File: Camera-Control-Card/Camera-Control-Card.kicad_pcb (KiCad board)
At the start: 4 copper layers, 65 x 41.6 mm, 129 parts, among them J1 SFV24R-1STE1HLF, J2 Conn_02x05_Counter_Clockwise, J3 Conn_Coaxial, J4 Conn_Coaxial, J5 Conn_Coaxial, J6 Conn_Coaxial, J7 Conn_Coaxial, J8 10018784-10201TLF, J9 USB_C_Receptacle_USB2.0_16P, U1 LCMXO2-7000HC-6TG144I, U2 T602-025.0M, U3 SN74LVC1G125DRL, U4 74AHC125, U5 74AHC125, U6 TPD2EUSB30, U7 CP2102N-Axx-xQFN20, U8 SN74LVC1G125DRL

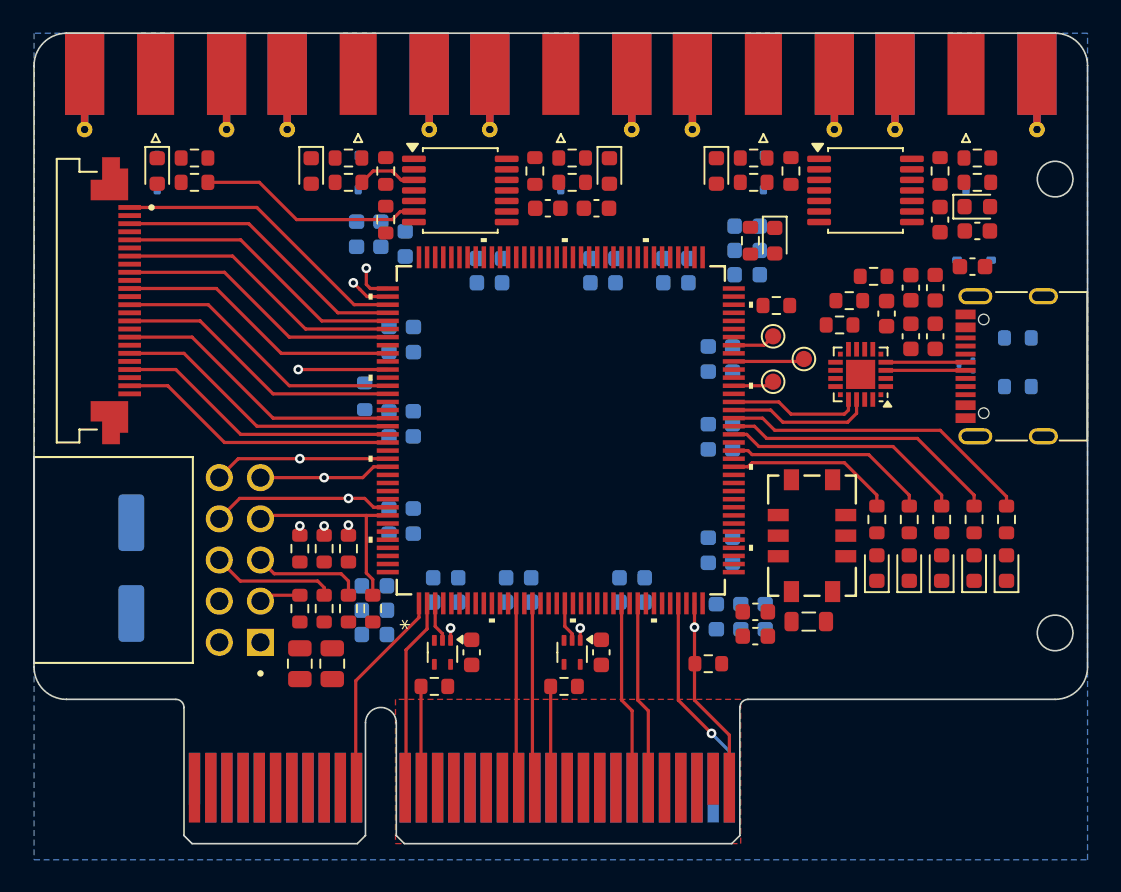
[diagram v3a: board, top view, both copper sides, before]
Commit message: Layout completed for camera control card
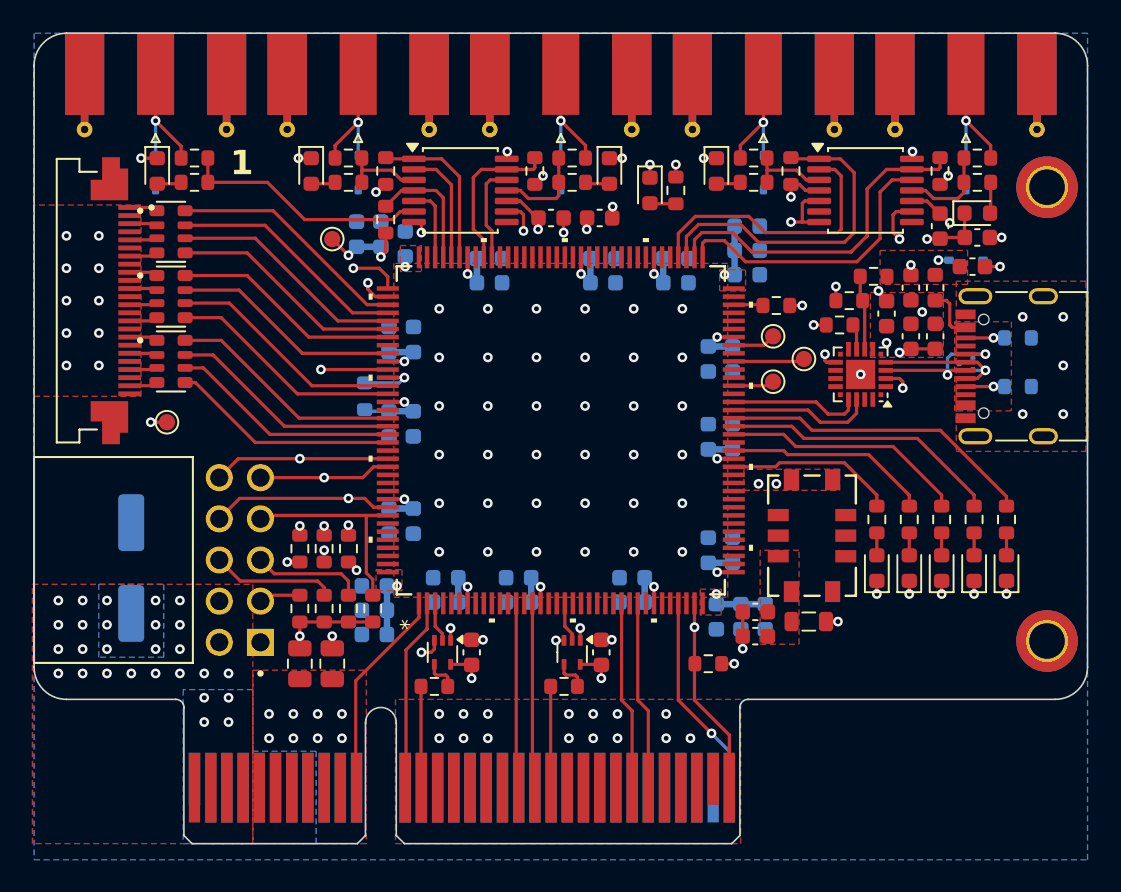
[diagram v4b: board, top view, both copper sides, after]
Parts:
- added H1: MountingHole_Pad, MountingHole:MountingHole_2.2mm_M2_DIN965_Pad_TopBottom, F.Cu at (182.5, 88.5)
- added H2: MountingHole_Pad, MountingHole:MountingHole_2.2mm_M2_DIN965_Pad_TopBottom, F.Cu at (182.5, 116.5)
- added RN1: EXB-38V330JV, Footprints:RESCAXS80P320X160X60-8N, F.Cu at (128.4, 91.2)
- added RN2: EXB-38V330JV, Footprints:RESCAXS80P320X160X60-8N, F.Cu at (128.4, 95.2)
- added RN3: EXB-38V330JV, Footprints:RESCAXS80P320X160X60-8N, F.Cu at (128.4, 99.2)
- added TP4: TestPoint, TestPoint:TestPoint_Pad_D1.0mm, F.Cu at (138.4, 91.7)
- added TP5: TestPoint, TestPoint:TestPoint_Pad_D1.0mm, F.Cu at (128.2, 103.0)
- C47: value 1uF -> 0.1uF
- moved D17 8.30 mm to (158.0, 88.7)
- moved R6 5.55 mm to (159.6, 88.7)
- moved C43 0.63 mm to (154.9, 90.4)
- moved C44 0.63 mm to (151.9, 90.4)
- moved D15 0.50 mm to (177.5, 93.0)
- moved C46 0.40 mm to (175.9, 90.9)
- moved C45 0.40 mm to (178.2, 91.6), turned to 180 degrees
- moved D13 0.40 mm to (178.2, 90.1)
- moved D9 0.10 mm to (127.5, 87.6)
- moved U6 0.10 mm to (177.5, 99.4)
- turned R30 to 180 degrees
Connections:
- J1 pad 1: /FPGA/PT35B -> Net-(J1-Pad1)
- J1 pad 11: /FPGA/PT28A -> Net-(J1-Pad11)
- J1 pad 13: /FPGA/PT25B -> Net-(J1-Pad13)
- J1 pad 15: /FPGA/PT25A -> Net-(J1-Pad15)
- J1 pad 17: /FPGA/PT22D -> Net-(J1-Pad17)
- J1 pad 19: /FPGA/PT22C -> Net-(J1-Pad19)
- J1 pad 21: /FPGA/PT18B -> Net-(J1-Pad21)
- J1 pad 23: /FPGA/PT18A -> Net-(J1-Pad23)
- J1 pad 3: /FPGA/PT35A -> Net-(J1-Pad3)
- J1 pad 5: /FPGA/PT33B -> Net-(J1-Pad5)
- J1 pad 7: /FPGA/PT33A -> Net-(J1-Pad7)
- J1 pad 9: /FPGA/PT28B -> Net-(J1-Pad9)
- U1 pad 100: unconnected-(U1B-PR5A-Pad100) -> /Buffer_3V3/OE_2
- U1 pad 103: unconnected-(U1B-PR4C-Pad103) -> /Buffer_3V3/OE_1
- U1 pad 104: unconnected-(U1B-PR3B-Pad104) -> /Buffer_3V3/IN_1
- U1 pad 105: unconnected-(U1B-PR3A-Pad105) -> /Buffer_3V3/OE_0
- U1 pad 106: unconnected-(U1B-PR2B-Pad106) -> /Buffer_3V3/IN_0
- U1 pad 61: /FPGA/CS -> unconnected-(U1A-PB31A-Pad61)
- U1 pad 73: unconnected-(U1B-PR24B-Pad73) -> /Buffer_3V3/IN_4
- U1 pad 74: unconnected-(U1B-PR24A-Pad74) -> /Buffer_3V3/OE_4
- U1 pad 75: unconnected-(U1B-PR23B-Pad75) -> /Buffer_3V3/OE_3
- U1 pad 76: unconnected-(U1B-PR23A-Pad76) -> /Buffer_3V3/IN_3
- U1 pad 99: unconnected-(U1B-PR5B-Pad99) -> /Buffer_3V3/IN_2
- U5 pad 11: unconnected-(U5-Pad11) -> Net-(R30-Pad2)
- U5 pad 12: GND -> /Buffer_3V3/IN_4
- U5 pad 13: +3V3 -> /Buffer_3V3/OE_4
- U5 pad 4: /Buffer_3V3/OE_4 -> +3V3
- U5 pad 5: /Buffer_3V3/IN_4 -> GND
- U5 pad 6: Net-(R30-Pad2) -> unconnected-(U5-Pad6)
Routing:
- net +3V3: track 0.00 -> 67.6 mm, vias 0 -> 68
- net GND: track 0.00 -> 35.2 mm, vias 0 -> 108
- net /Buffer_3V3/OE_4: track 0.00 -> 21.4 mm
- net /Buffer_3V3/OE_3: track 0.00 -> 20.6 mm
- net /Buffer_3V3/IN_4: track 0.00 -> 18.2 mm
- net /Buffer_3V3/IN_3: track 0.00 -> 17.3 mm
- net /Buffer_3V3/OE_1: track 0.00 -> 10.0 mm
- net /Buffer_3V3/OE_2: track 0.00 -> 9.87 mm
- net /Buffer_3V3/OUT_0: track 0.00 -> 8.00 mm, vias 0 -> 1
- net /Buffer_3V3/OUT_4: track 0.00 -> 7.98 mm, vias 0 -> 1
- net /Buffer_3V3/OUT_2: track 0.00 -> 7.98 mm, vias 0 -> 1
- net /Buffer_3V3/OUT_3: track 0.00 -> 7.84 mm, vias 0 -> 1
- net /Buffer_3V3/OUT_1: track 0.00 -> 7.84 mm, vias 0 -> 1
- net /Buffer_3V3/OE_0: track 0.00 -> 7.82 mm
- net /Buffer_3V3/IN_1: track 0.00 -> 7.18 mm
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- added copper zone on B.Cu, net +3V3
- added copper zone on F.Cu, net +3V3
- added copper zone on F.Cu, net /USB/VBUS
- added copper zone on F.Cu, net Net-(F1-Pad1)
- added copper zone on F.Cu, net Net-(U2-Enable/Disable)
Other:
- outline, holes or cut-outs redrawn
- board text added: "1"
